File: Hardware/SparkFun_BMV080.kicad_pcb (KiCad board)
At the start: 2 copper layers, 25.4 x 12.7 mm, 53 parts, among them J2 Qwiic_Vertical, J3 Conn_01x06, J4 Conn_01x01, U1 BMV080

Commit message: pre-review last second updates
-added VCC input requirements and ranges into sch
-added temp range to sch
-added pin 1 indicator silk to molex connector
-added extra GRND trace connection on pad 2 of molex connector
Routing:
- net GND: track 5.92 -> 6.63 mm
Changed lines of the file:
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@@
 				(font
 					(size 0.001 0.001)
+					(thickness 0.15)
 				)
 			)
@@
 				(font
 					(size 0.001 0.001)
+					(thickness 0.15)
 				)
 			)
@@
 		(tags "kb_params=eyJBbGlnbm1lbnRDaG9pY2UiOiAiQ2VudGVyIiwgIkNhcExlZnRDaG9pY2UiOiAiWyIsICJDYXBSaWdodENob2ljZSI6ICIpIiwgIkZvbnRDb21ib0JveCI6ICJGcmVkZHlTcGFyay1SZWd1bGFyIiwgIkhlaWdodEN0cmwiOiAwLjksICJMYXllckNvbWJvQm94IjogIkYuU2lsa1MiLCAiTGluZVNwYWNpbmdDdHJsIjogMC44LCAiTXVsdGlMaW5lVGV4dCI6ICJCTVYwODAiLCAiUGFkZGluZ0JvdHRvbUN0cmwiOiAxLjAsICJQYWRkaW5nTGVmdEN0cmwiOiAyLjUsICJQYWRkaW5nUmlnaHRDdHJsIjogMi41LCAiUGFkZGluZ1RvcEN0cmwiOiAxLjAsICJXaWR0aEN0cmwiOiAwLjEsICJhZHZhbmNlZENoZWNrYm94IjogdHJ1ZSwgImlubGluZUZvcm1hdFRleHRib3giOiB0cnVlLCAibGluZW92ZXJTdHlsZUNob2ljZSI6ICJTcXVhcmUiLCAibGluZW92ZXJUaGlja25lc3NDdHJsIjogMX0=")
 		(property "Reference" "kibuzzard-66BFB450"
-			(at 0 -3.516026 360)
+			(at 0 -3.516026 0)
 			(layer "F.SilkS")
 			(hide yes)
@@
 		)
 		(property "Value" "G***"
-			(at 0 3.516026 360)
+			(at 0 3.516026 0)
 			(layer "F.SilkS")
 			(hide yes)
@@
 		)
 		(property "Footprint" ""
-			(at 0 0 360)
+			(at 0 0 0)
 			(layer "F.Fab")
 			(hide yes)
@@
 		)
 		(property "Datasheet" ""
-			(at 0 0 360)
+			(at 0 0 0)
 			(layer "F.Fab")
 			(hide yes)
@@
 		)
 		(property "Description" ""
-			(at 0 0 360)
+			(at 0 0 0)
 			(layer "F.Fab")
 			(hide yes)
@@
 			(layer "F.SilkS")
 		)
+		(fp_circle
+			(center 1.811 1.856)
+			(end 1.705 1.77)
+			(stroke
+				(width 0.1)
+				(type default)
+			)
+			(fill solid)
+			(layer "F.SilkS")
+		)
 		(fp_rect
 			(start -3.08 -1.567)
@@
 		)
 		(group ""
-			(members "057b338e-3c59-47b2-9586-1703aa589c1e" "0cd8f99f-60f5-40b1-bab0-e3d4ed010b88"
-				"1f841cc6-05cf-4e3d-905f-9fbde8dbccfb" "215496e4-c3fd-49d7-a6de-b309c23c3580"
-				"39ef52a8-1bc8-47c3-824f-7e11211b15cd" "42d42824-b0c0-4a45-97e2-2b39fa5bfd8c"
-				"4f291738-8a0f-4412-b18c-d16bf4c76e58" "6ab3c432-37a7-435e-af0f-852af69405cb"
-				"80b25020-8392-46dc-ba4d-ab70394c2f9e" "860965eb-83b0-4206-9e38-fe425dfb2a16"
-				"bad00dfb-07c5-464a-adb4-cb9d809d876d" "de6ce91f-0a80-4492-bf31-298e0291b662"
-				"f76bf74f-a426-4feb-91a4-6135452c1ac8" "fb10baaa-9d9e-4226-bd99-2d9ce95dc66d"
+			(members "37416548-1bf1-4119-8dc2-92a195c4bb3c" "3c0b9990-796d-4ec5-bc29-c8a8b6a97a98"
+				"4fc5cdca-e298-4f24-b624-0cd3c875ec3d" "58b5df87-8235-4716-9a1c-f74071808e55"
+				"62efbbdd-33d8-4ade-a410-e8de906fa856" "80e106e8-33e1-4912-a6e4-6e94437e82ea"
+				"a80fe231-93db-4d5e-8935-149bb3947811" "ab2dff78-7074-452a-9e0f-b3143281634f"
+				"ace14e2a-8068-4c16-8443-d787f0821350" "b89fff30-6715-4976-934b-a3e9da6b2bb1"
+				"be331db5-0191-452c-9401-65f44dbd0514" "e305b98b-0636-419a-9185-ee59a0068213"
+				"f17ad507-3af0-4b3a-adfc-0d09c1d06d41" "fc12405f-1b2b-40ae-a43a-07ec4ab177b3"
 			)
 		)
@@
 				(font
 					(size 0.001 0.001)
+					(thickness 0.15)
 				)
 			)
@@
 				(font
 					(size 0.001 0.001)
+					(thickness 0.15)
 				)
 			)
@@
 		)
 		(height -13.97)
-		(gr_text "0.1 in"
+		(gr_text "2.54 mm"
 			(at 116.332707 114.172865 0)
 			(layer "Dwgs.User")
@@
 		)
 		(height 5.08)
-		(gr_text "0.1 in"
+		(gr_text "2.54 mm"
 			(at 139.149934 105.41 0)
 			(layer "Dwgs.User")
@@
 		)
 		(height 11.43)
-		(gr_text "1.0000 in"
+		(gr_text "25.4000 mm"
 			(at 129.54 77.59 0)
 			(layer "Dwgs.User")
@@
 		)
 		(height -5.08)
-		(gr_text "0.5 in"
+		(gr_text "12.7 mm"
 			(at 110.61 96.52 90)
 			(layer "Dwgs.User")
@@
 		)
 		(height 5.73)
-		(gr_text "0.078 in"
+		(gr_text "1.97 mm"
 			(at 116.139583 85.027562 0)
 			(layer "Dwgs.User")
@@
 		)
 		(height -5.08)
-		(gr_text "0.1 in"
+		(gr_text "2.54 mm"
 			(at 144.698765 103.560373 90)
 			(layer "Dwgs.User")
@@
 		)
 		(height -7.62)
-		(gr_text "0.1 in"
+		(gr_text "2.54 mm"
 			(at 126.412525 109.208426 0)
 			(layer "Dwgs.User")
@@
 		)
 		(height 7.094373)
-		(gr_text "0.026 in"
+		(gr_text "0.654 mm"
 			(at 146.05 89.26239 89.97669108)
 			(layer "Dwgs.User")
@@
 		)
 		(height 5.08)
-		(gr_text "0.1 in"
+		(gr_text "2.54 mm"
 			(at 114.191139 103.378036 90)
 			(layer "Dwgs.User")
@@
 		)
 		(height -10.16)
-		(gr_text "0.2500 in"
+		(gr_text "6.3500 mm"
 			(at 116.240553 111.685379 0)
 			(layer "Dwgs.User")
@@
 		)
 		(height 12.17)
-		(gr_text "0.248 in"
+		(gr_text "6.3 mm"
 			(at 151.13 90.17 90)
 			(layer "Dwgs.User")
@@
 		)
 		(height -9.54)
-		(gr_text "0.79 in"
+		(gr_text "20.14 mm"
 			(at 128.89 80.13 0)
 			(layer "Dwgs.User")
@@
 		(height 10.1)
 		(orientation 0)
-		(gr_text "0.046 in"
+		(gr_text "1.17 mm"
 			(at 140.317477 107.887092 0)
 			(layer "Dwgs.User")
@@
 		(height 7.52)
 		(orientation 1)
-		(gr_text "0.198 in"
+		(gr_text "5.02 mm"
 			(at 148.59 103.575005 90)
 			(layer "Dwgs.User")
@@
 		(width 0.2032)
 		(layer "F.Cu")
+		(net 3)
+	)
+	(segment
+		(start 119.285 92.48)
+		(end 119.997955 92.48)
+		(width 0.2032)
+		(layer "F.Cu")

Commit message: sensor position outline correction and more
-added F.Fab and F.Silk outline for sensor - to help with correctly showing position on PCB
-changed PROD_ID to connector for the sensor
-made v01 in copper "knockout" style
-adjusted F.Mask to match the area of the sensor we are supposed to use thermal tape on
-adjusted B.Mask to match our small heat sink.
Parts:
- moved kibuzzard-66BFB450 11.6 mm to (129.2, 91.0)
- moved kibuzzard-66C4B812 3.09 mm to (138.6, 91.0), turned to 0 degrees
- moved kibuzzard-66C4B81D 0.05 mm to (141.1, 93.9)
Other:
- board text added: "Finish: HASL Lead-free"
- board text removed: "Finish: HAL Lead-free"

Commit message: added SFE and OSHW logos
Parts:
- added G***: LOGO, SparkFun-Aesthetic:SparkFun_Logo_NoFlame_5mm, F.Cu at (125.4, 91.1)
- added Ref**: Val**, SparkFun-Aesthetic:OSHW_Logo_2.5mm, B.Cu at (121.3, 98.6)
- moved kibuzzard-66BFB450 1.76 mm to (131.0, 91.0)

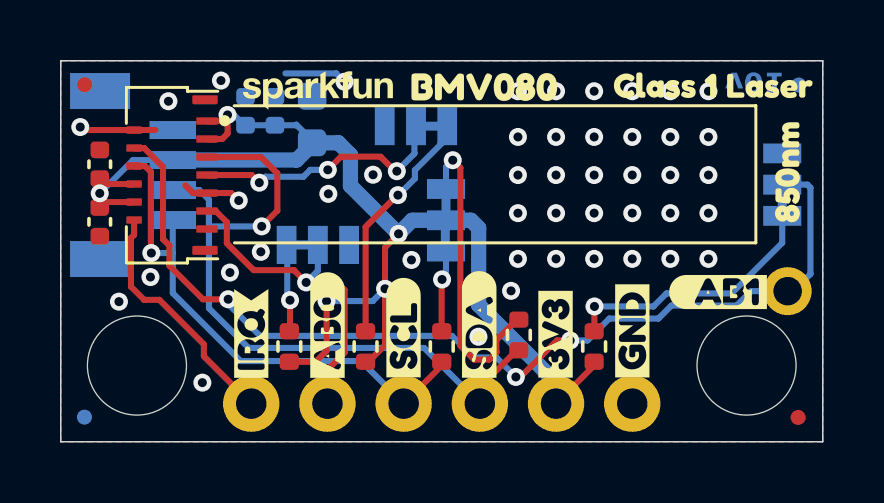
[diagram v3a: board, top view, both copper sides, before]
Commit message: dimensions update and resistor line up
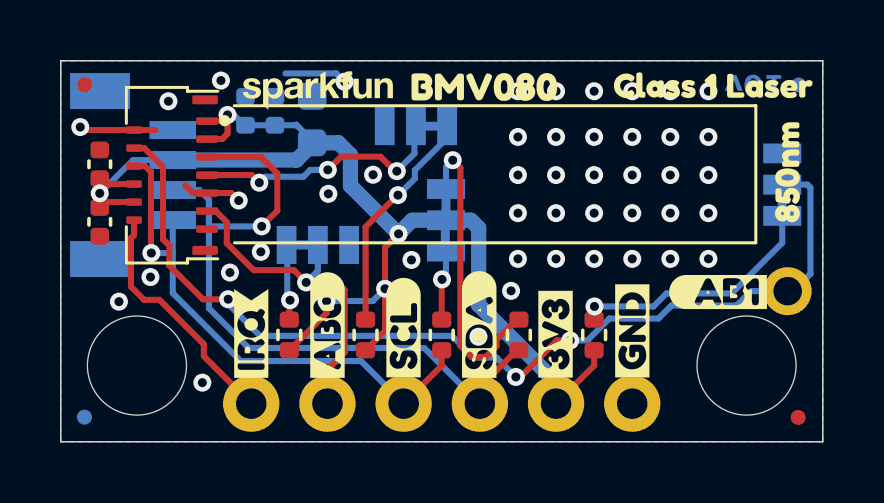
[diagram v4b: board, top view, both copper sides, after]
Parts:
- moved R1 0.38 mm to (127.0, 99.3)
- moved R2 0.38 mm to (124.5, 99.3)
- moved R3 0.38 mm to (129.5, 99.3)
- moved R4 0.38 mm to (134.6, 99.3)
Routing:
- net 3.3V: track 43.4 -> 42.4 mm

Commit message: moved AB1/CS header onto 0.5 grid for perf board/breadboard
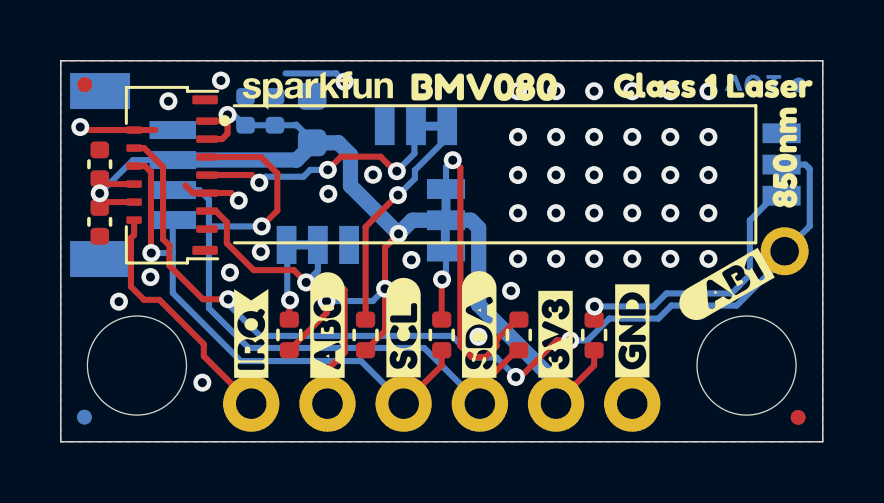
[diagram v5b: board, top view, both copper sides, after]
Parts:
- moved J4 1.33 mm to (141.0, 96.5)
- moved kibuzzard-66C3B30A 0.75 mm to (140.9, 95.3)
- moved JP3 0.67 mm to (140.9, 93.6)
- moved kibuzzard-66C3B2FA 0.65 mm to (140.8, 91.8)
- moved kibuzzard-66C3B31E 0.61 mm to (139.7, 93.6)
- moved kibuzzard-66C4B81D 0.49 mm to (141.0, 93.4)
- moved kibuzzard-66BFC321 0.46 mm to (139.3, 97.5), turned to -150 degrees
- moved kibuzzard-66BFC29E 0.26 mm to (138.9, 97.7), turned to 30 degrees
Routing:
- net Net-(JP3-A): track 8.48 -> 9.28 mm

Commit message: checklist run eng
-sch tightening
-sch jumpers text notes
-set solder mask expansion to 0.05mm
-added active low line on top of CS label silk
-SCL silk label set to input end flag type
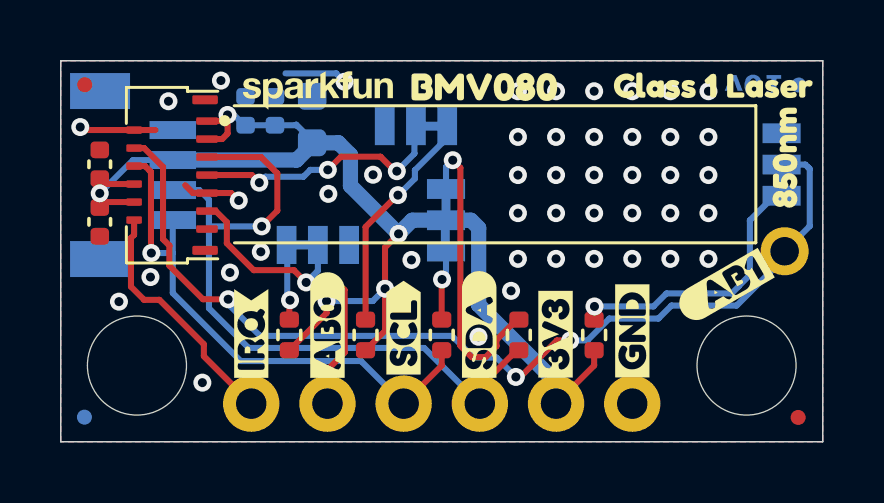
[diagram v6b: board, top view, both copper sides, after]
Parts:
- removed kibuzzard-66BFBF4E: G***, kibuzzard-66BFBF4E
- removed kibuzzard-66BFC321: G***, kibuzzard-66BFC321
- added kibuzzard-66C77290: G***, kibuzzard-66C77290, B.Cu at (139.3, 97.5)
- added kibuzzard-66C772E5: G***, kibuzzard-66C772E5, F.Cu at (128.3, 99.1)
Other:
- rule pad_to_mask_clearance: 0 -> 0.05
